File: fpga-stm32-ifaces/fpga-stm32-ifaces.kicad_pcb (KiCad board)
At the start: 6 copper layers, 90 x 94.5 mm, 274 parts, among them J1 0826-1G1T-23-F, J10 CORTEX_DEBUG_ETM, J11 XILINX_JTAG, J12 CONN_01X03, J2 PMOD_HOST, J3 PMOD_HOST, J4 XILINX_JTAG, J5 CONN_01X03, J6 CONN_01X03, J7 CONN_PCIE_PWR_8PIN, J8 XILINX_JTAG, J9 CONN_IBC_MGMT_DEVICE, M1 LOGO, M2 LOGO, M3 LOGO, M5 SCREWHOLE, M6 SCREWHOLE, M7 SCREWHOLE, M8 SCREWHOLE, U1 STM32H735-UFBGA176-25, U10 ECS-1612MV-250-CN, U11 STM32L431-QFN48, U12 MUN12AD03-SE, U13 MUN12AD03-SE, U14 MUN12AD03-SE, U15 MUN12AD03-SE, U16 W25Q128JV, U2 XC7S25-1FTGB196, U3 S25FL128SAGBHIA10, U4 KSZ9031RN, U5 RCLAMP0514M, U6 RCLAMP0514M, U7 ECS-1612MV-250-CN, U8 AT24MAC402, U9 ECS-1612MV-250-CN

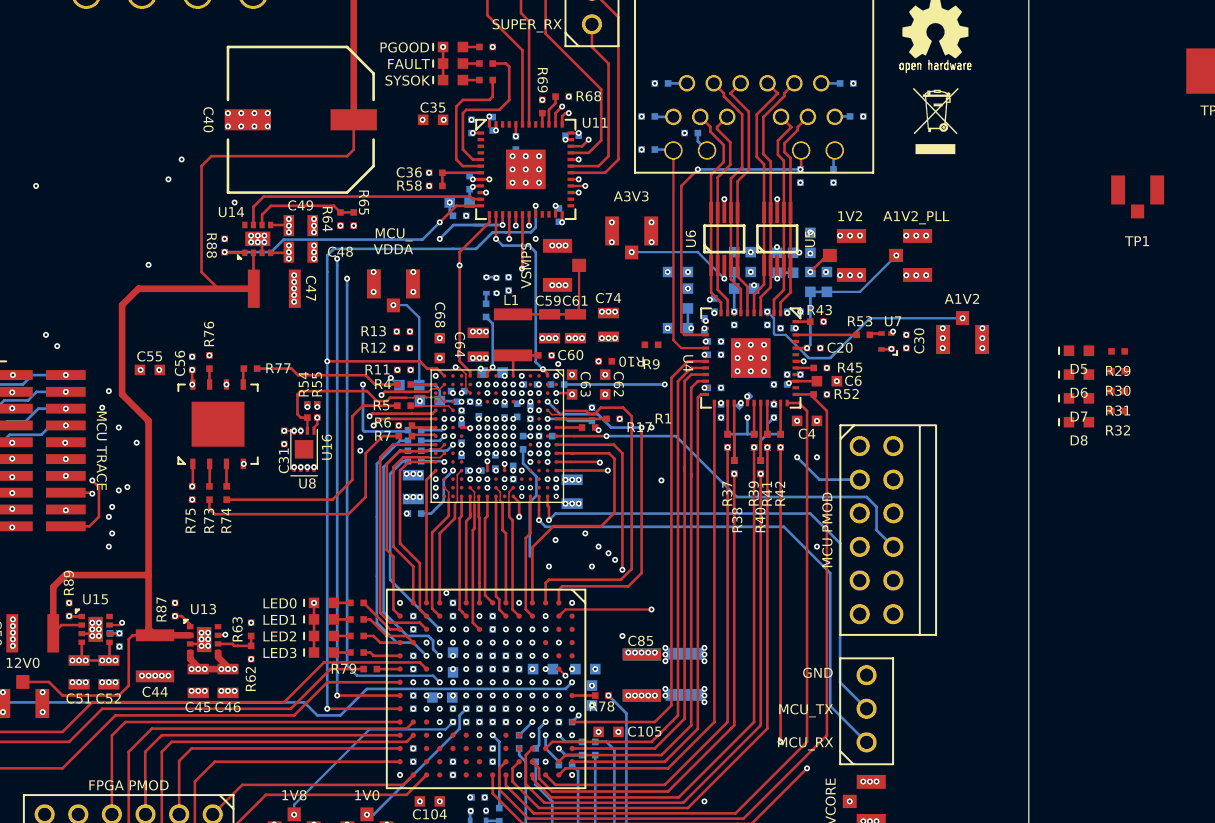
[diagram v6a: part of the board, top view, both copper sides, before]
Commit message: Finished FPGA and MCU escape and interconnect routing
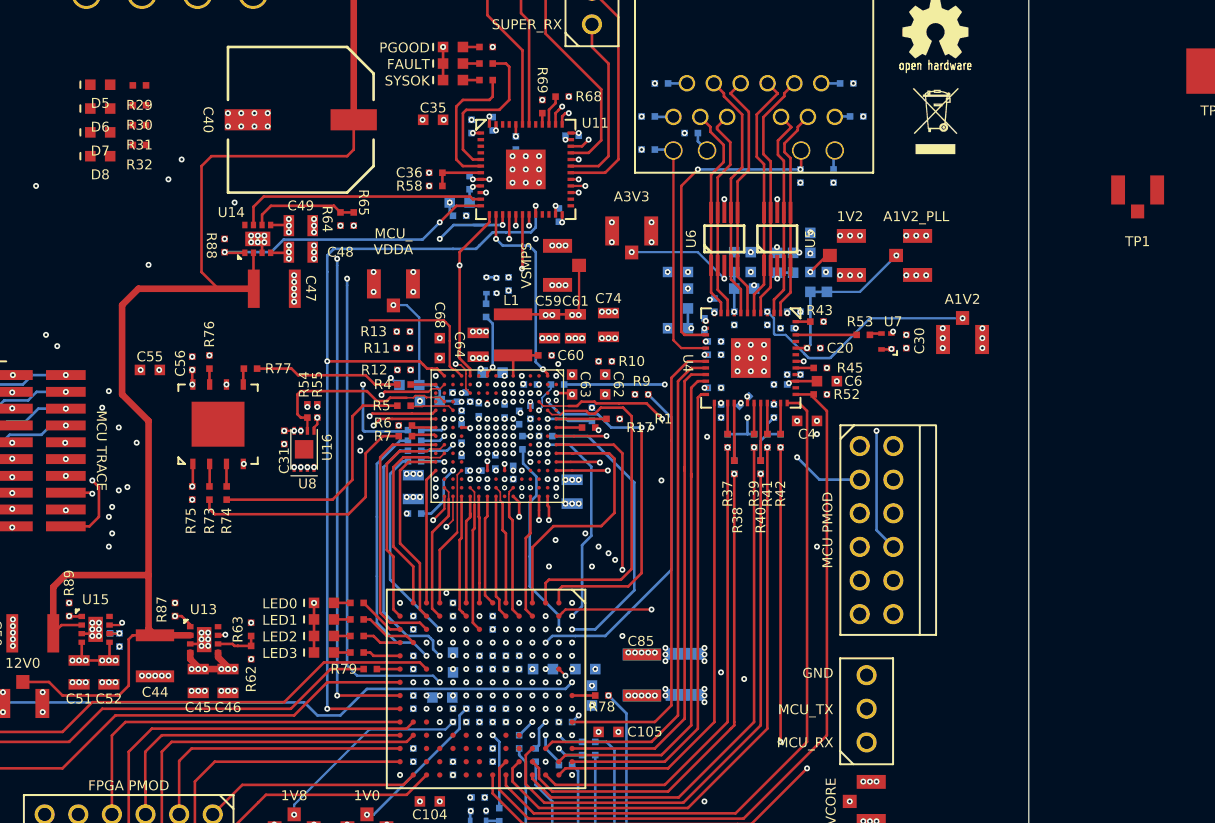
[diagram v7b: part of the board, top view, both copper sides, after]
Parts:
- moved D5 76.6 mm to (47.9, 67.3)
- moved D6 76.6 mm to (47.9, 69.2)
- moved D7 76.6 mm to (47.9, 71.0)
- moved D8 76.6 mm to (47.9, 72.8)
- moved R29 76.6 mm to (50.8, 67.4)
- moved R30 76.6 mm to (50.8, 68.9)
- moved R31 76.6 mm to (50.8, 70.4)
- moved R32 76.6 mm to (50.8, 71.9)
- moved R9 3.82 mm to (88.8, 90.8), turned to 180 degrees
- moved R11 1.65 mm to (70.8, 87.2)
- moved R12 1.65 mm to (70.8, 88.9)
- moved C75 0.57 mm to (79.5, 92.5)
- moved C80 0.14 mm to (75.0, 90.6)
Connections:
- U1 pad H1: /MCU/MCU_LED_0 -> unconnected-(U1F-PF6-PadH1)
- U1 pad J2: /MCU/MCU_LED_2 -> unconnected-(U1F-PF8-PadJ2)
- U1 pad J3: /MCU/MCU_LED_1 -> unconnected-(U1F-PF7-PadJ3)
- U1 pad J4: /MCU/MCU_LED_3 -> /MCU/MCU_LED_2
- U1 pad M1: unconnected-(U1C-PC2-PadM1) -> /MCU/MCU_LED_3
- U1 pad N15: unconnected-(U1H-PH12-PadN15) -> /MCU/MCU_LED_0
- U1 pad P15: unconnected-(U1H-PH6-PadP15) -> /MCU/MCU_LED_1
- U2 pad A3: /MCU/FPGA_QSPI_CS_N -> /MCU/FPGA_QSPI_DQ6
- U2 pad A5: /MCU/FPGA_QSPI_DQ6 -> /MCU/FMC_NBL1
- U2 pad B3: /MCU/FPGA_QSPI_DQ0 -> /MCU/FPGA_QSPI_CS_N
- U2 pad B5: /MCU/FMC_NBL1 -> /MCU/FPGA_QSPI_DQ1
- U2 pad B6: /MCU/FPGA_QSPI_DQ3 -> /MCU/FPGA_QSPI_DQ2
- U2 pad C4: /MCU/FPGA_QSPI_DQ1 -> /MCU/FPGA_QSPI_DQ0
- U2 pad C5: /MCU/FPGA_QSPI_DQ2 -> /MCU/FPGA_QSPI_DQ3
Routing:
- net /MCU/FPGA_QSPI_DQ1: track 0.00 -> 44.5 mm, vias 0 -> 3
- net /MCU/FMC_NBL1: track 0.00 -> 44.1 mm, vias 0 -> 4
- net /MCU/MCU_PMOD_DQ2: track 0.00 -> 39.8 mm
- net /MCU/FMC_NOE: track 0.00 -> 29.6 mm, vias 1 -> 2
- net /MCU/MCU_PMOD_DQ6: track 1.74 -> 31.1 mm
- net /MCU/FPGA_QSPI_DQ0: track 0.00 -> 25.8 mm, vias 0 -> 2
- net /MCU/FPGA_QSPI_DQ6: track 0.00 -> 21.7 mm, vias 0 -> 1
- net /MCU/FMC_NWE: track 0.00 -> 15.9 mm, vias 1 -> 2
- net /MCU/MCU_LED_2: track 0.00 -> 14.8 mm
- net /MCU/MCU_LED_0: track 0.00 -> 13.9 mm, vias 0 -> 1
- net /MCU/MCU_LED_1: track 0.00 -> 11.8 mm
- net /MCU/MCU_LED_3: track 0.00 -> 10.5 mm
- net Net-(U1F-PF0): track 0.00 -> 10.3 mm, vias 0 -> 2
- net /Power support/VSMPS: track 33.9 -> 43.3 mm, vias 5 -> 9
- net Net-(U1F-PF1): track 0.00 -> 9.20 mm
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
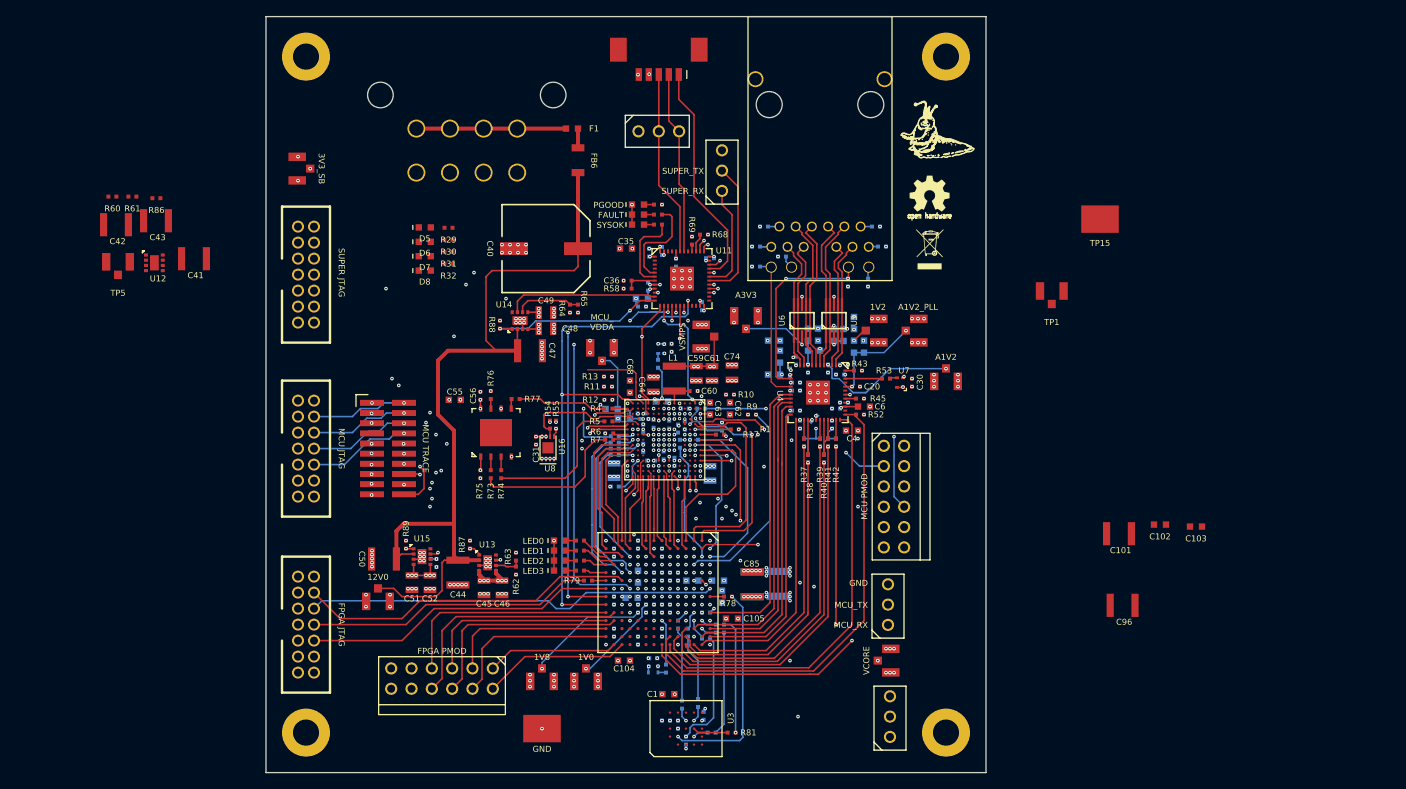
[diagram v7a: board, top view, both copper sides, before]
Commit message: Finished initial layout, passing DRC
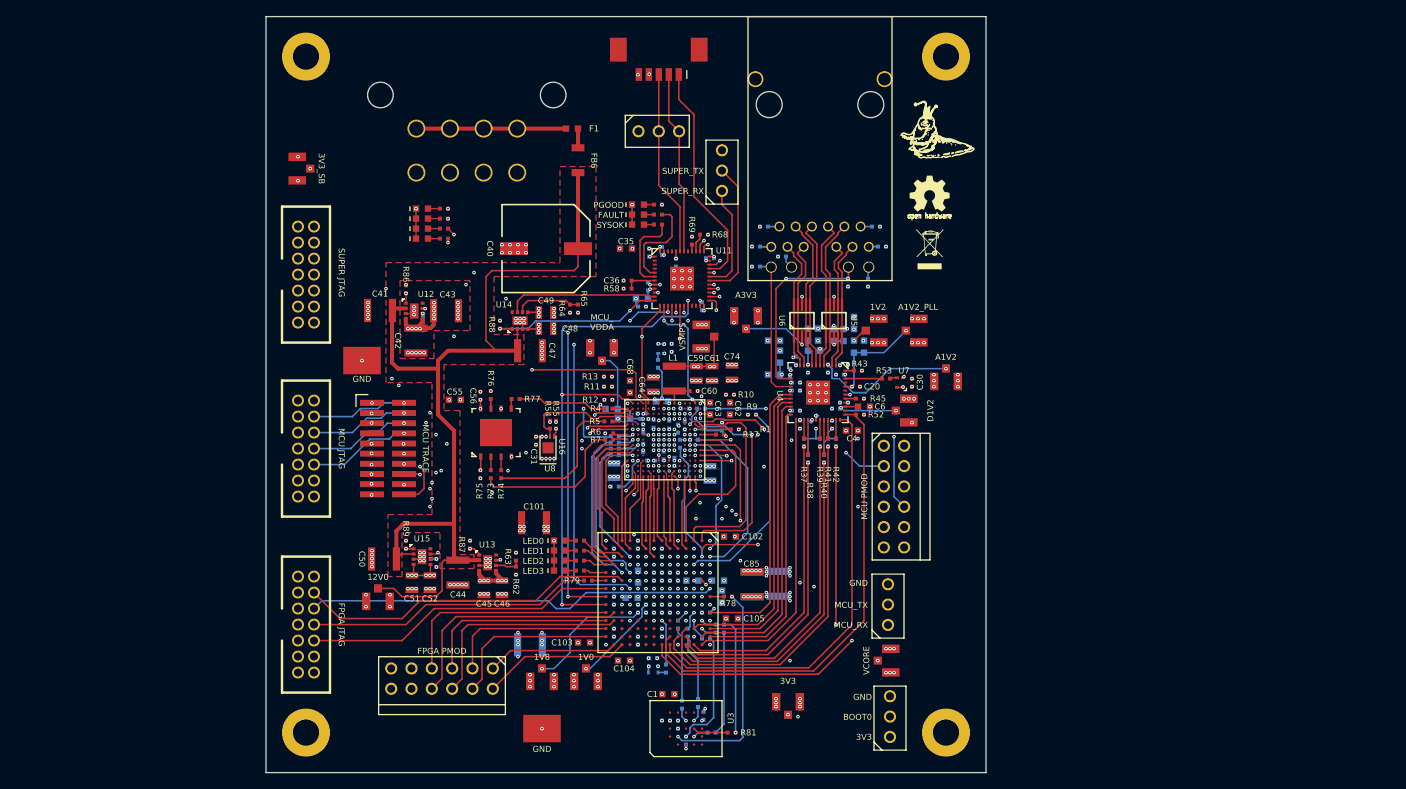
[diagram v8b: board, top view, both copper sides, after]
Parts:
- C96, R60, R61: moved to B.Cu
- moved TP5 100.2 mm to (93.2, 126.8)
- moved TP15 93.9 mm to (40.0, 84.0)
- moved C103 77.9 mm to (67.8, 119.2), turned to 180 degrees
- moved C96 74.2 mm to (61.0, 119.5), turned to 180 degrees
- moved C101 73.1 mm to (61.5, 104.2)
- moved C102 53.8 mm to (86.0, 106.0)
- moved R60 42.0 mm to (47.6, 79.7), turned to 90 degrees
- moved C42 40.2 mm to (46.8, 81.5), turned to -90 degrees
- moved R61 38.8 mm to (47.1, 78.4), turned to 180 degrees
- moved C43 38.0 mm to (50.5, 77.8)
- moved R86 33.2 mm to (45.5, 75.1), turned to 90 degrees
- moved U12 33.0 mm to (46.5, 77.8)
- moved C41 24.1 mm to (42.2, 77.8), turned to 180 degrees
- moved TP1 23.3 mm to (108.2, 90.2), turned to -90 degrees
- moved D8 4.02 mm to (47.5, 68.8)
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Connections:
- U1 pad J4: /MCU/MCU_LED_2 -> /MCU/MCU_LED_1
- U1 pad M1: /MCU/MCU_LED_3 -> /MCU/MCU_LED_0
- U1 pad N15: /MCU/MCU_LED_0 -> /MCU/MCU_LED_2
- U1 pad P15: /MCU/MCU_LED_1 -> /MCU/MCU_LED_3
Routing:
- net /GND: track 993.5 -> 1077.2 mm, vias 347 -> 388
- net /Power supply/3V3_EN: track 0.00 -> 47.3 mm, vias 0 -> 2
- net /3V3: track 417.4 -> 461.5 mm, vias 71 -> 87
- net /MCU/MCU_LED_3: track 10.5 -> 54.1 mm, vias 0 -> 3
- net /MCU/MCU_LED_1: track 11.8 -> 54.3 mm, vias 1 -> 3
- net /Power supply/3V3_PGOOD: track 0.00 -> 40.9 mm, vias 0 -> 2
- net /MCU/MCU_LED_2: track 14.8 -> 54.0 mm, vias 1 -> 3
- net /MCU/MCU_LED_0: track 13.9 -> 41.9 mm, vias 1 -> 2
- net /12V0: track 106.1 -> 120.8 mm
- net /Power supply/1V8: track 61.0 -> 67.8 mm, vias 15 -> 18
- net /Ethernet/D1V2: track 19.2 -> 25.6 mm, vias 7 -> 8
- net /Power support/VCORE: track 65.3 -> 71.6 mm
- net /Ethernet/1V2: track 56.3 -> 54.4 mm
- net /Ethernet/A1V2: track 27.3 -> 25.7 mm
- net Net-(D8-A): track 0.00 -> 1.50 mm
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- added copper zone on F.Cu, net /12V0
- added copper zone on In4.Cu, net /3V3
- added copper zone on In4.Cu, net /Ethernet/1V2
- added copper zone on In4.Cu, net /Ethernet/A3V3
- added copper zone on In4.Cu, net /Ethernet/D1V2
- added copper zone on In1.Cu, net /GND
- added copper zone on In4.Cu, net /Power supply/1V0
- added copper zone on In4.Cu, net /Power supply/1V8
- added copper zone on In4.Cu, net /Power supply/3V3_SB
- added copper zone on In4.Cu, net /Power support/VCORE
- added copper zone on In4.Cu, net /Power support/VSMPS
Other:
- board text added: "3V3"
- board text added: "BOOT0"
- board text added: "D1V2"
